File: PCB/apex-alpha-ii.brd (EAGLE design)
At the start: 100 x 80 mm, 36 parts, among them IC1 CC430F5135, IC2 TPS61200, Y1 26MHz

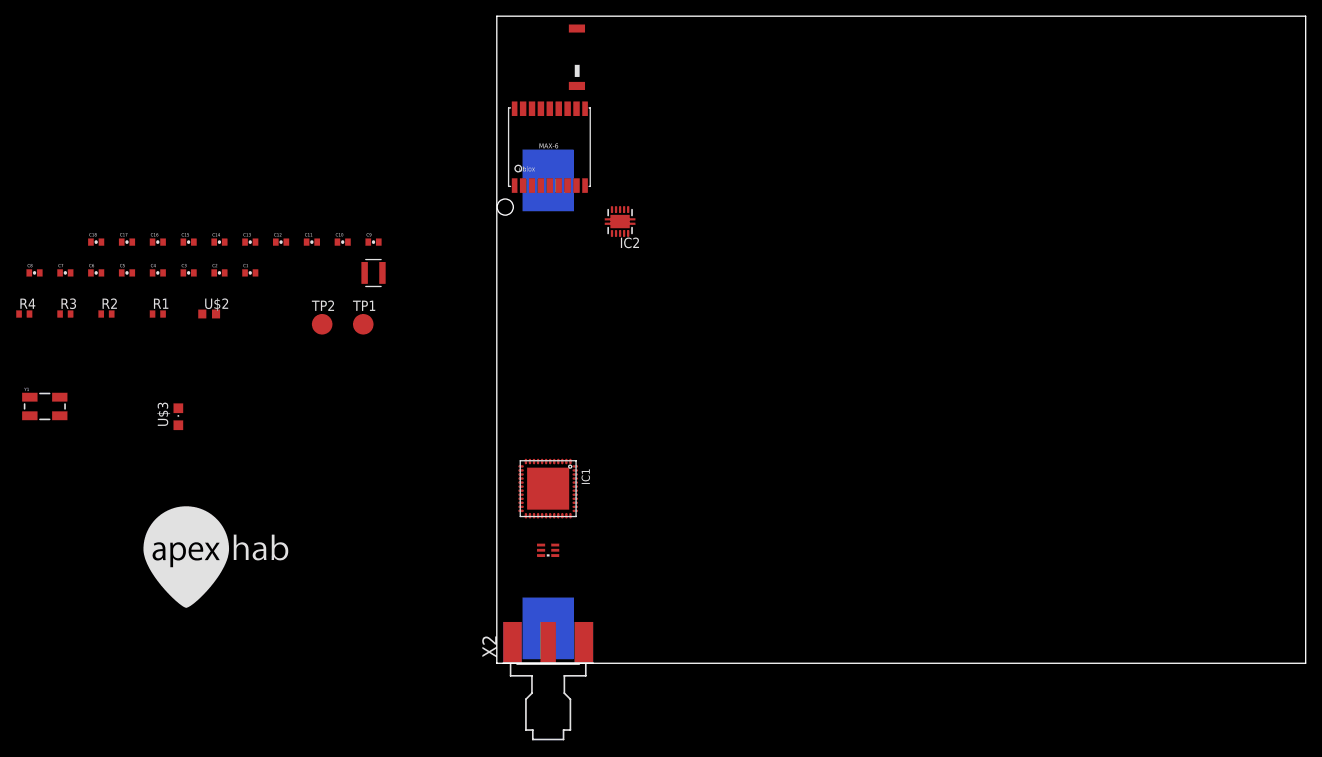
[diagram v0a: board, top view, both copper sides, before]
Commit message: Flipped battery - still AAA
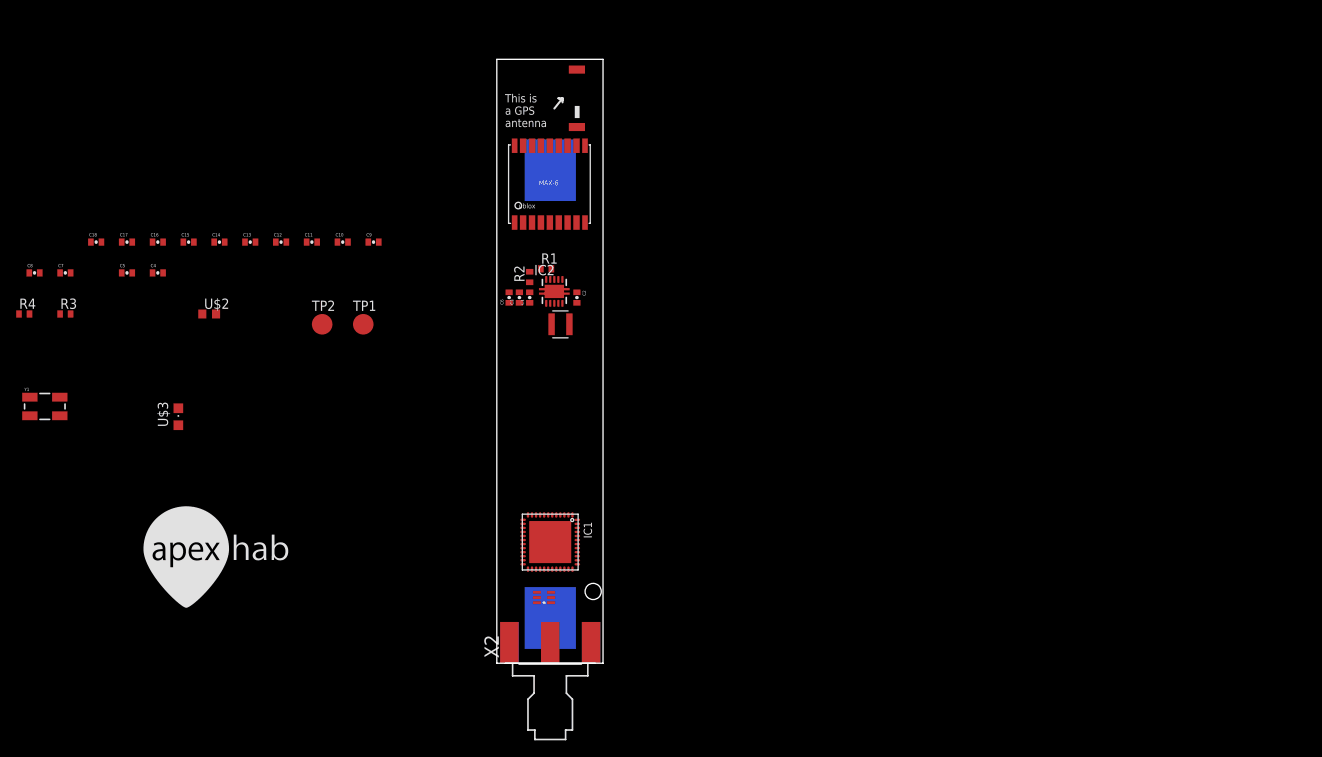
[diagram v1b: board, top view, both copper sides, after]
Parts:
- X2: device con-coax:J502-ND-142-0711-871/876 -> !danielparts:J502-ND-142-0701-801/806
- moved R2 52.5 mm to (4.06, 47.8), turned to 90 degrees
- moved C6 51.1 mm to (1.52, 45.2), turned to 90 degrees
- moved R1 48.3 mm to (6.10, 48.8)
- moved C2 44.3 mm to (9.91, 45.2), turned to 270 degrees
- moved C3 41.0 mm to (2.79, 45.2), turned to 90 degrees
- moved C1 34.7 mm to (4.06, 45.2), turned to 90 degrees
- moved NR3015 24.0 mm to (7.87, 41.9)
- moved IC2 11.9 mm to (7.11, 46.0), turned to 0 degrees
- moved IC1 6.61 mm to (6.60, 15.0)
- moved F1 5.86 mm to (5.84, 8.13)
- moved U$1 5.08 mm to (8.64, 70.1)
- moved GPS 4.57 mm to (6.60, 59.4)
- moved AAA 1.30 mm to (6.60, 33.3), turned to 90 degrees
- moved X2 0.25 mm to (6.60, 0.00)
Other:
- board size 100 x 80 mm -> 13.1 x 74.7 mm
- board text added: "This is a GPS antenna"
